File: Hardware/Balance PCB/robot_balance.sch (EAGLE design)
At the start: 47 parts, among them Q1 16Mhz

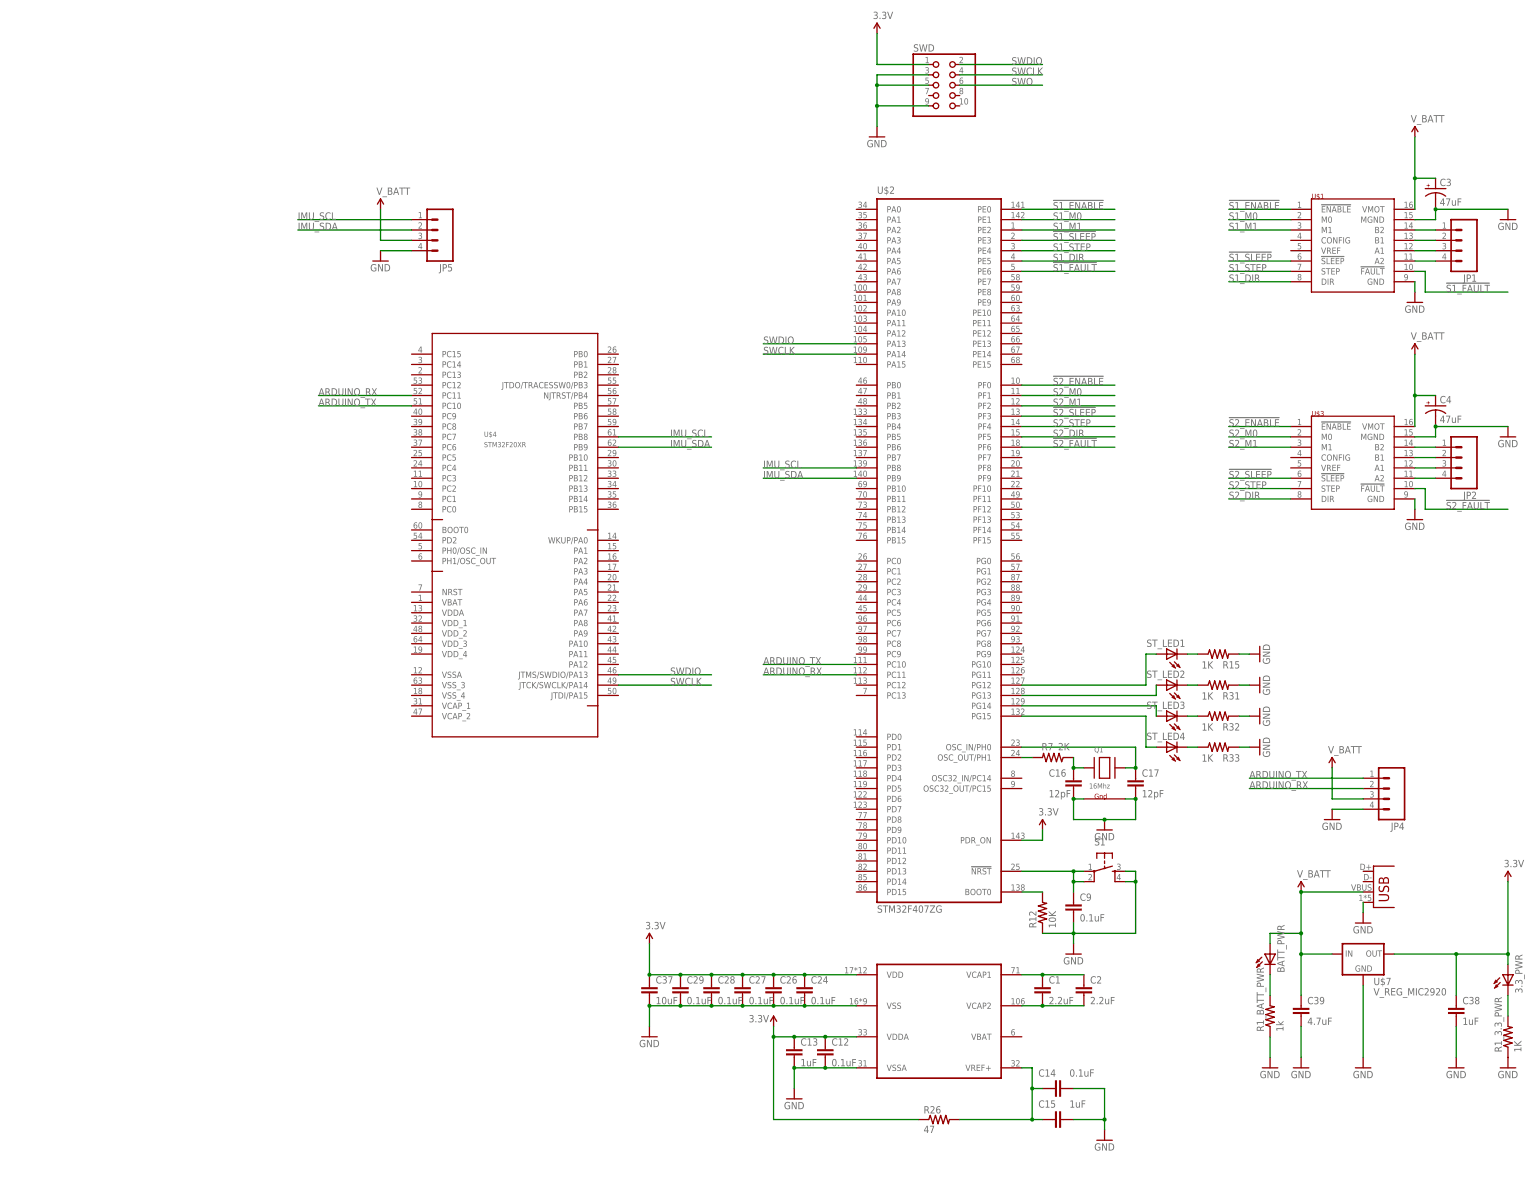
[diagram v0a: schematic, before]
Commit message: Replaced 144 pin Balancing MCU with smaller 64 pin version and added a .gitignore file
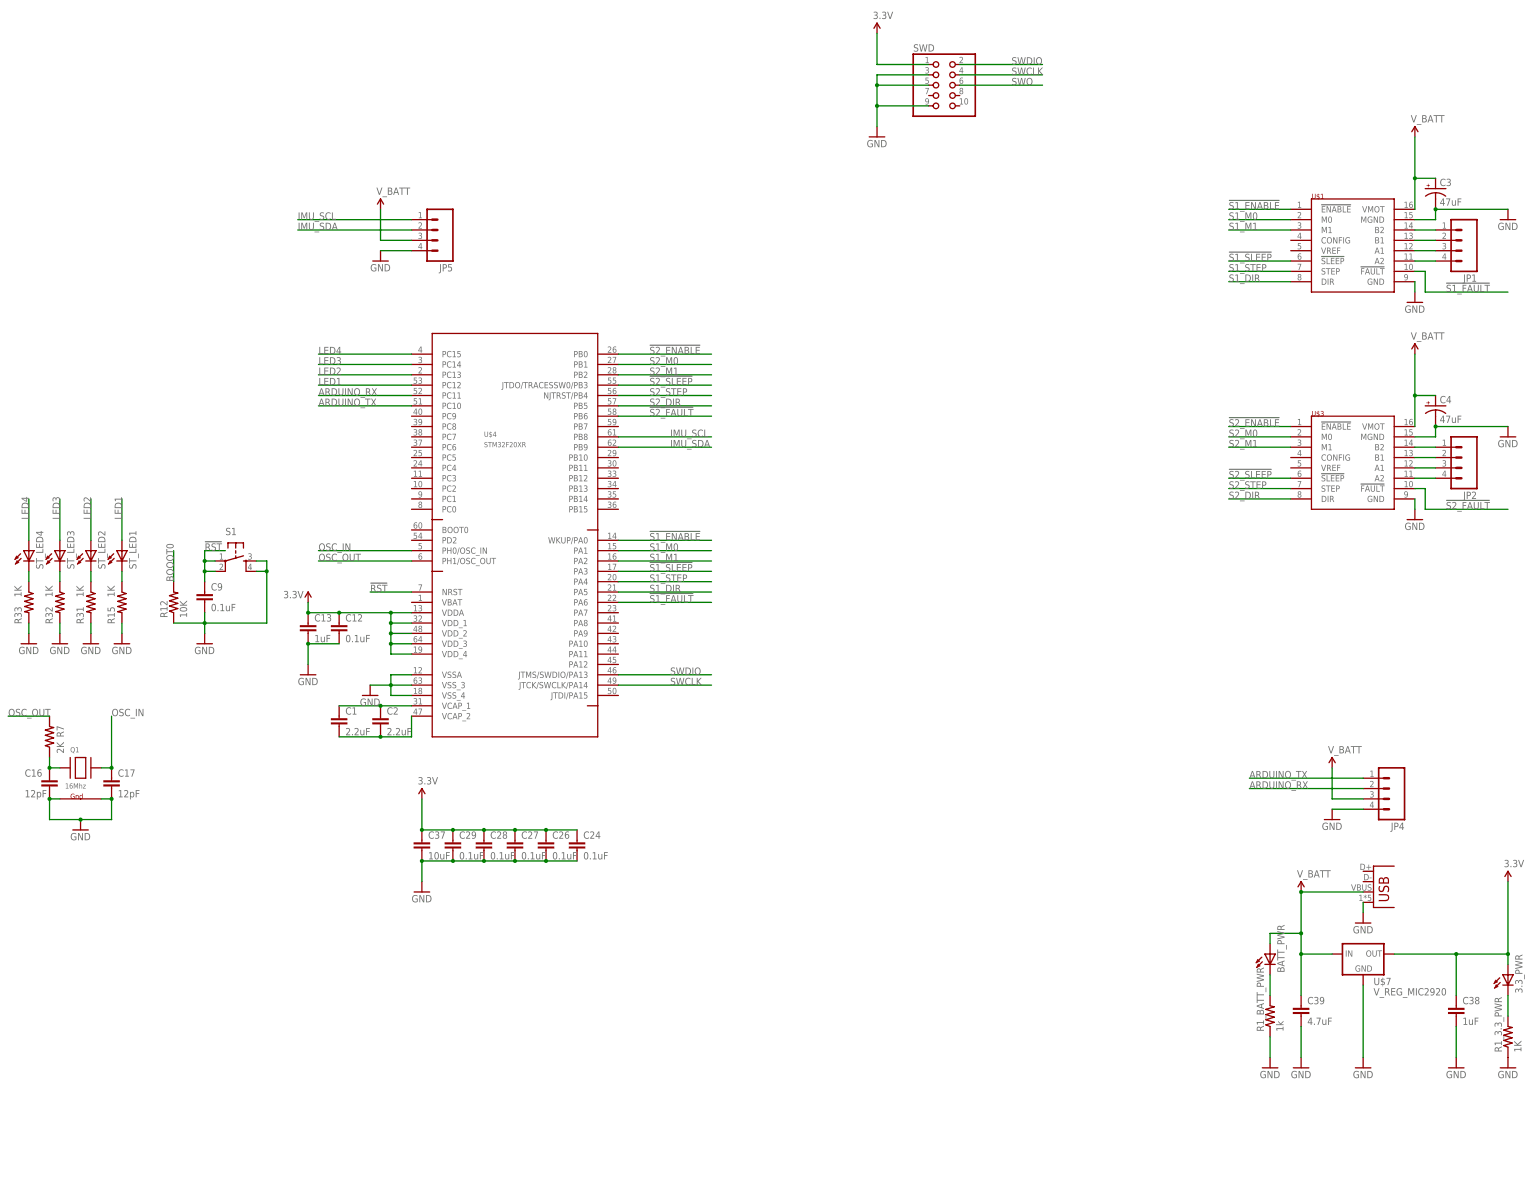
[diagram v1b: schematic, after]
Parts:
- removed C14: 0.1uF, SparkFun-Capacitors:2.2UF-25V-+80/-20(0805)
- removed C15: 1uF, SparkFun-Capacitors:2.2UF-25V-+80/-20(0805)
- removed R26: 47, SparkFun-Passives:RESISTOR0805-RES
- removed U$2: STM32F407ZG, CAMERA:STM32F407ZG
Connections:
- removed net N$10: C9.1, S1.1, S1.2, U$2.!NRST
- removed net N$11: R12.2, U$2.BOOT0
- removed net N$14: C14.1, C15.1, R26.2, U$2.VREF+
- removed net N$15: C17.1, Q1.X2, U$2.OSC_IN/PH0
- removed net N$22: R7.2, U$2.OSC_OUT/PH1
- removed net N$42: ST_LED1.A, U$2.PG12
- removed net N$44: ST_LED2.A, U$2.PG13
- removed net N$46: ST_LED3.A, U$2.PG14
- removed net N$48: ST_LED4.A, U$2.PG15
- new net !RST: C9.1, S1.1, S1.2, U$4.NRST
- new net BOOOT0: R12.2
- new net LED1: ST_LED1.A, U$4.PC12
- new net LED2: ST_LED2.A, U$4.PC13
- new net LED3: ST_LED3.A, U$4.PC14
- new net LED4: ST_LED4.A, U$4.PC15
- new net OSC_IN: C17.1, Q1.X2, U$4.PH0/OSC_IN
- new net OSC_OUT: R7.2, U$4.PH1/OSC_OUT
- net !S1_ENABLE: now also U$4.WKUP/PA0; no longer U$2.PE0
- net !S1_FAULT: now also U$4.PA6; no longer U$2.PE6
- net !S1_SLEEP: now also U$4.PA3; no longer U$2.PE3
- net !S2_ENABLE: now also U$4.PB0; no longer U$2.PF0
- net !S2_FAULT: now also U$4.PB6; no longer U$2.PF6
- net !S2_SLEEP: now also U$4.JTDO/TRACESSW0/PB3; no longer U$2.PF3
- net 3.3V: now also U$4.VDDA, U$4.VDD_1, U$4.VDD_2, U$4.VDD_3, U$4.VDD_4; no longer R26.1, U$2.PDR_ON, U$2.VDD, U$2.VDDA
- net ARDUINO_RX: now also U$4.PC11; no longer U$2.PC11
- net ARDUINO_TX: now also U$4.PC10; no longer U$2.PC10
- net GND: now also U$4.VSSA, U$4.VSS_3, U$4.VSS_4; no longer C14.2, C15.2, U$2.VSS, U$2.VSSA
- net IMU_SCL: now also U$4.PB8; no longer U$2.PB8
- net IMU_SDA: now also U$4.PB9; no longer U$2.PB9
- net N$12: now also U$4.VCAP_2; no longer U$2.VCAP2
- net N$2: now also U$4.VCAP_1; no longer U$2.VCAP1
- net S1_DIR: now also U$4.PA5; no longer U$2.PE5
- net S1_M0: now also U$4.PA1; no longer U$2.PE1
- net S1_M1: now also U$4.PA2; no longer U$2.PE2
- net S1_STEP: now also U$4.PA4; no longer U$2.PE4
- net S2_DIR: now also U$4.PB5; no longer U$2.PF5
- net S2_M0: now also U$4.PB1; no longer U$2.PF1
- net S2_M1: now also U$4.PB2; no longer U$2.PF2
- net S2_STEP: now also U$4.NJTRST/PB4; no longer U$2.PF4
- net SWCLK: now also U$4.JTCK/SWCLK/PA14; no longer U$2.PA14
- net SWDIO: now also U$4.JTMS/SWDIO/PA13; no longer U$2.PA13
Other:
- moved on the sheet: C1, C12, C13, C16, C17, C2, C24, C26, C27, C28, C29, C37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

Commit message: Added FTDI USB to Serial Converter as ALI suggested
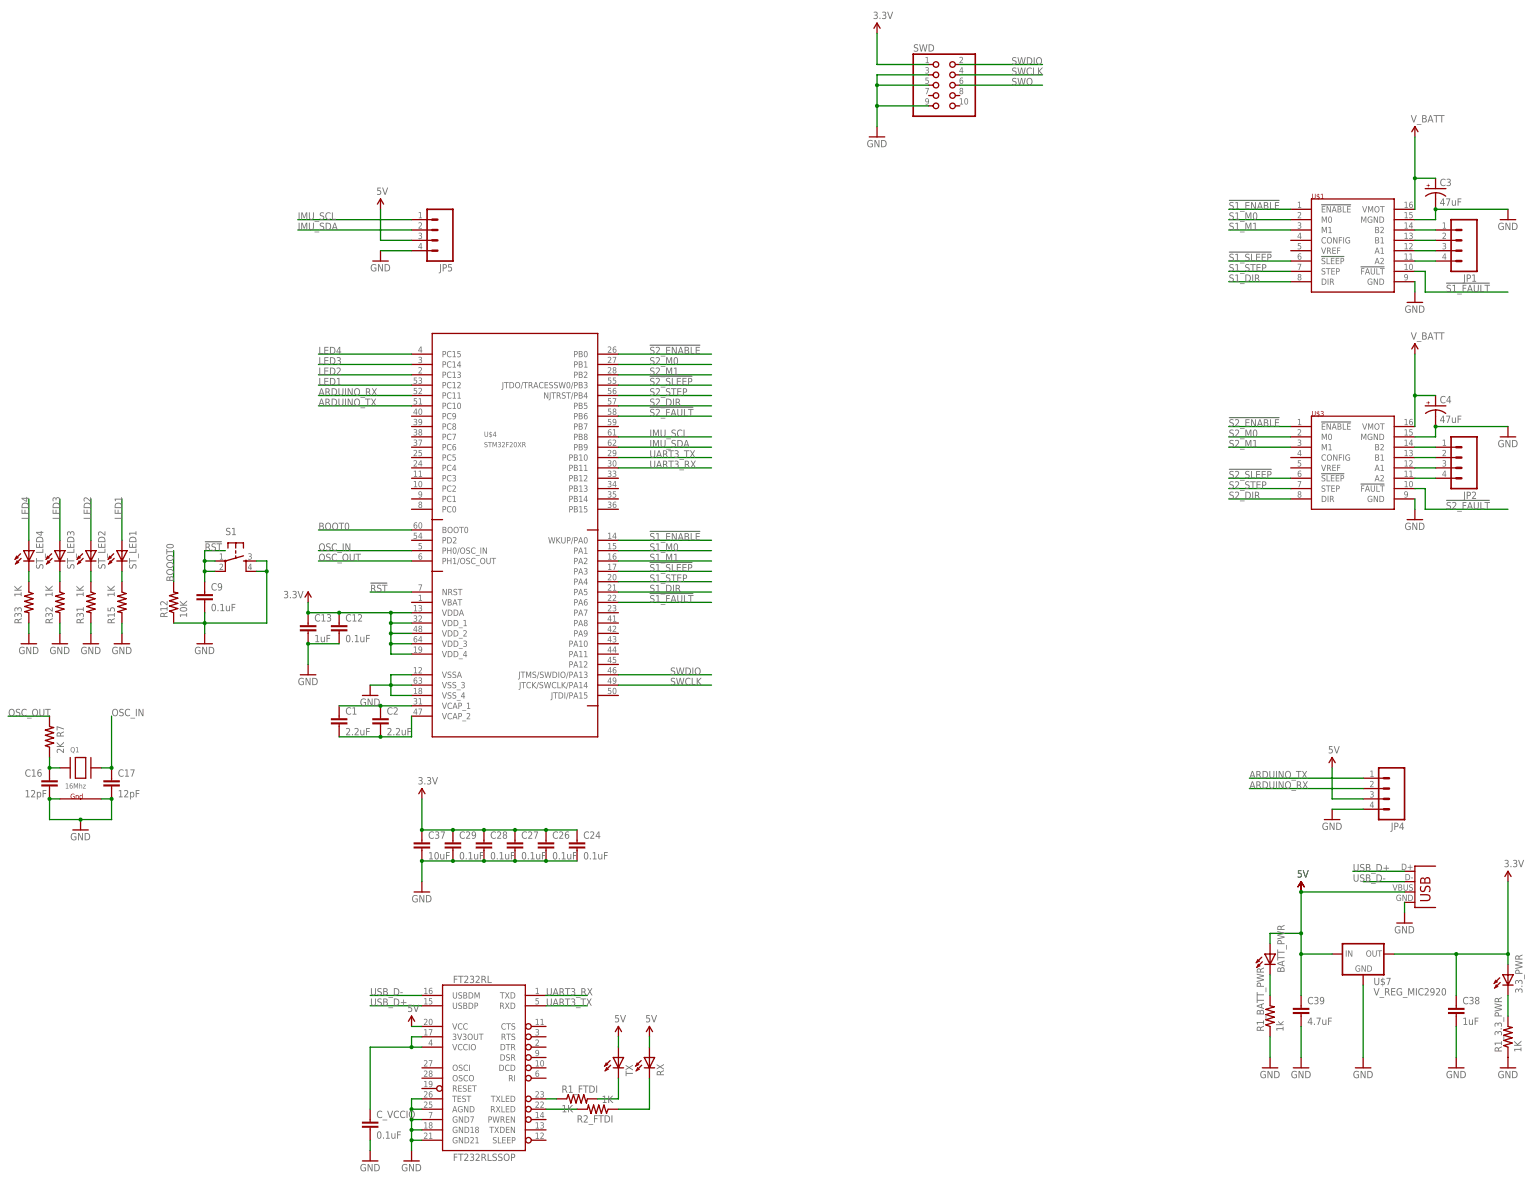
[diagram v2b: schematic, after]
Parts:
- added C_VCCIO: 0.1uF, SparkFun-Capacitors:CAP0603-CAP
- added FT232RL: FT232RLSSOP, SparkFun-DigitalIC:FT232RLSSOP
- added R1_FTDI, R2_FTDI: 1K, SparkFun-Passives:RESISTOR0603-RES
- added RX, TX: (no value), adafruit:LEDCHIPLED_0805
- ST_LED1, ST_LED2, ST_LED3, ST_LED4: device LilyPad-Wearables:LED1206 -> adafruit:LEDCHIPLED_0805
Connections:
- removed net V_BATT: JP4.3, JP5.3
- new net 5V: BATT_PWR.A, C39.1, FT232RL.VCC, JP3.VBUS, JP4.3, JP5.3, RX.A, TX.A, U$7.IN
- new net BOOT0: U$4.BOOT0
- new net N$10: FT232RL.RXLED, R2_FTDI.2
- new net N$11: R2_FTDI.1, RX.C
- new net N$13: C_VCCIO.1, FT232RL.3V3OUT, FT232RL.VCCIO
- new net N$8: FT232RL.TXLED, R1_FTDI.1
- new net N$9: R1_FTDI.2, TX.C
- new net UART3_RX: FT232RL.TXD, U$4.PB11
- new net UART3_TX: FT232RL.RXD, U$4.PB10
- new net USB_D+: FT232RL.USBDP, JP3.D+
- new net USB_D-: FT232RL.USBDM, JP3.D-
- net GND: now also C_VCCIO.2, FT232RL.AGND, FT232RL.GND18, FT232RL.GND21, FT232RL.GND7, FT232RL.TEST
- net V_USB: no longer BATT_PWR.A, C39.1, JP3.VBUS, U$7.IN
